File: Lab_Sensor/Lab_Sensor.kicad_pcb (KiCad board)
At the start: 2 copper layers, 94.2 x 66 mm, 31 parts, among them U1 ESP32-POE, U2 AM2302, U3 SSD1306, U4 INMP441

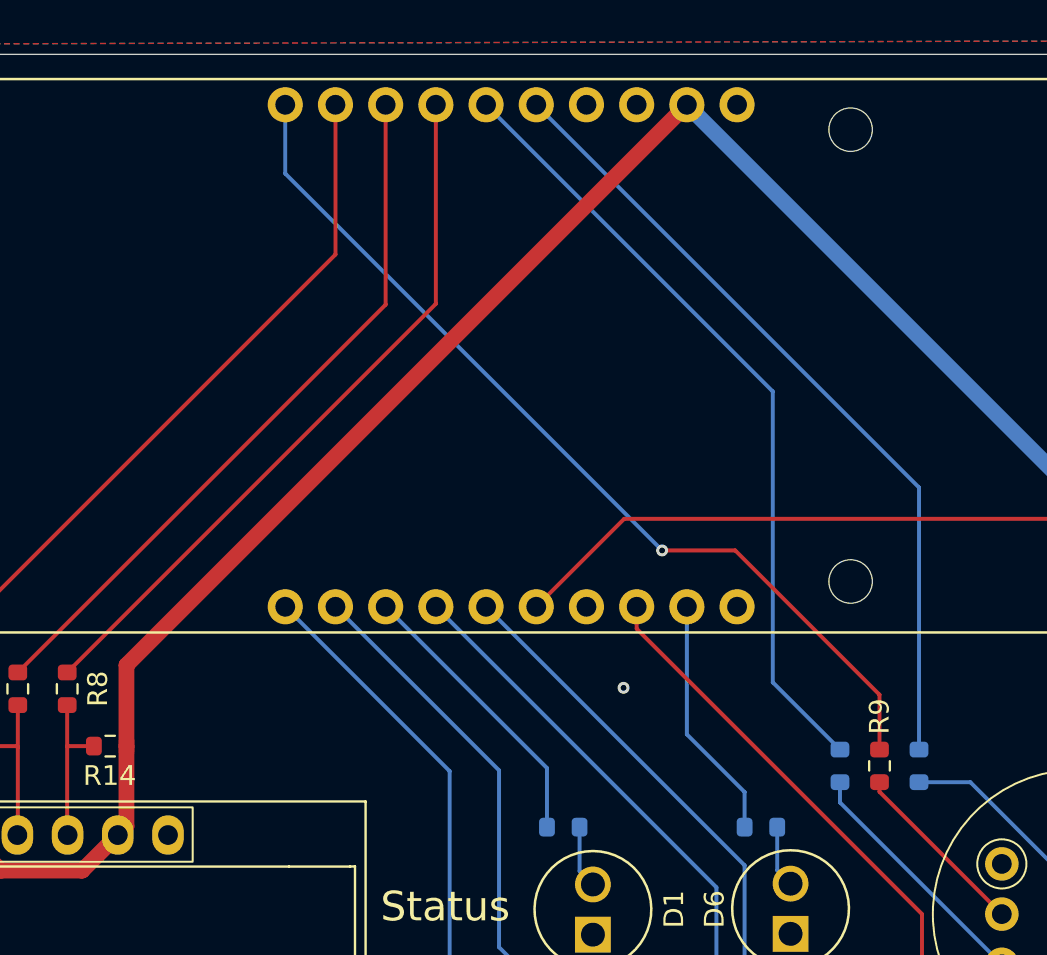
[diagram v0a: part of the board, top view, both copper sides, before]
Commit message: rerouted Input GPIO pins & added YAML file
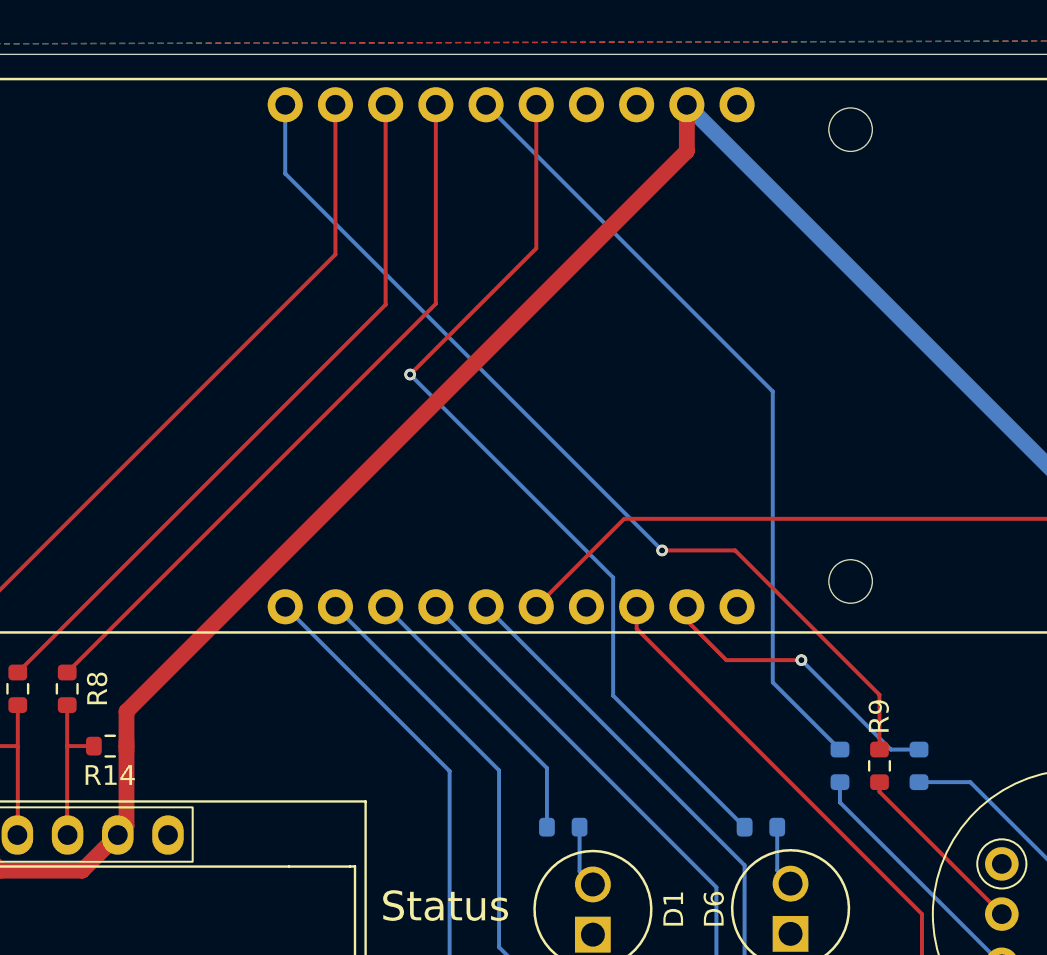
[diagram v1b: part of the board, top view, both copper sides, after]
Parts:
- turned R12 to 180 degrees
- turned R6 to -90 degrees
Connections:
- R12 pad 1: Net-(U1-GPI36) -> Net-(D6-PadA)
- R12 pad 2: Net-(D6-PadA) -> Net-(U1-GPIO0)
- R6 pad 1: Net-(U4-SD) -> Net-(U1-GPI36)
- R6 pad 2: Net-(U1-GPIO0) -> Net-(U4-SD)
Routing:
- net Net-(U1-GPIO0): track 40.6 -> 46.2 mm, vias 0 -> 1
- net Net-(U1-GPI36): track 12.4 -> 15.2 mm, vias 0 -> 1
- net GND: vias 1 -> 0

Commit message: switched pin 5 and 36
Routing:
- net GND: vias 0 -> 1
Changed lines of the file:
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@@
 		(net 1)
+	)
+	(via
+		(at 114.35 77.2)
+		(size 0.6)
+		(drill 0.3)
+		(layers "F.Cu" "B.Cu")
+		(free yes)
+		(net 2)
 	)
 	(segment
@@
 	)
 	(segment
-		(start 116.023 72.973)
-		(end 116.023 78.948)
+		(start 115.95 78.875)
+		(end 122.675 85.6)
 		(width 0.2)
 		(layer "B.Cu")
@@
 	)
 	(segment
-		(start 116.023 78.948)
-		(end 122.675 85.6)
+		(start 105.75 62.7)
+		(end 115.95 72.9)
 		(width 0.2)
 		(layer "B.Cu")
@@
 	)
 	(segment
-		(start 105.75 62.7)
-		(end 116.023 72.973)
-		(width 0.2)
-		(layer "B.Cu")
+		(start 115.95 72.9)
+		(end 115.95 78.875)
+		(width 0.2)
+		(layer "B.Cu")

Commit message: Grounded L/R
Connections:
- R11 pad 2: Net-(U1-GPIO1) -> Net-(U1-GPIO4)
- TP2 pad TP: Net-(U1-GPIO4) -> Net-(U1-GPIO1)
- U4 pad 1: unconnected-(U4-L/R-Pad1) -> GND
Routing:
- net Net-(U1-GPIO1): track 40.0 -> 50.2 mm, vias 0 -> 1
- net Net-(U1-GPIO4): track 42.0 -> 43.2 mm
- net GND: vias 1 -> 3
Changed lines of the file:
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@@
 	(net 22 "Net-(D2-PadA)")
 	(net 23 "Net-(D3-PadA)")
-	(net 24 "unconnected-(U4-L{slash}R-Pad1)")
-	(net 25 "Net-(U1-GPI36)")
-	(net 26 "Net-(U1-GPI35)")
-	(net 27 "Net-(U4-SCK)")
-	(net 28 "Net-(U4-SD)")
-	(net 29 "Net-(D5-PadA)")
-	(net 30 "Net-(D6-PadA)")
-	(net 31 "Net-(U4-WS)")
-	(net 32 "Net-(U1-GPIO0)")
-	(net 33 "Net-(U1-GPIO1)")
+	(net 24 "Net-(U1-GPI36)")
+	(net 25 "Net-(U1-GPI35)")
+	(net 26 "Net-(U4-SCK)")
+	(net 27 "Net-(U4-SD)")
+	(net 28 "Net-(D5-PadA)")
+	(net 29 "Net-(D6-PadA)")
+	(net 30 "Net-(U4-WS)")
+	(net 31 "Net-(U1-GPIO0)")
+	(net 32 "Net-(U1-GPIO1)")
 	(footprint "Custom_Parts:5002"
 		(layer "F.Cu")
@@
 			(layers "*.Cu" "*.Mask")
 			(remove_unused_layers no)
-			(net 6 "Net-(U1-GPIO4)")
+			(net 32 "Net-(U1-GPIO1)")
 			(pintype "passive")
 			(solder_mask_margin 0.102)
@@
 			(layers "*.Cu" "*.Mask")
 			(remove_unused_layers no)
-			(net 24 "unconnected-(U4-L{slash}R-Pad1)")
+			(net 2 "GND")
 			(pinfunction "L/R")
-			(pintype "no_connect")
+			(pintype "power_in")
 		)
 		(pad "2" thru_hole circle
@@
 			(layers "*.Cu" "*.Mask")
 			(remove_unused_layers no)
-			(net 31 "Net-(U4-WS)")
+			(net 30 "Net-(U4-WS)")
 			(pinfunction "WS")
 			(pintype "input")
@@
 			(layers "*.Cu" "*.Mask")
 			(remove_unused_layers no)
-			(net 27 "Net-(U4-SCK)")
+			(net 26 "Net-(U4-SCK)")
 			(pinfunction "SCK")
 			(pintype "input")
@@
 			(layers "*.Cu" "*.Mask")
 			(remove_unused_layers no)
-			(net 28 "Net-(U4-SD)")
+			(net 27 "Net-(U4-SD)")
 			(pinfunction "SD")
 			(pintype "input")
 		)
 		(embedded_fonts no)
+		(model "C:/Users/sidko/Desktop/GitHub/PCB-Projects/KiCad/Misc/INMP441.step"
+			(offset
+				(xyz 0 0 1.5)
+			)
+			(scale
+				(xyz 1 1 1)
+			)
+			(rotate
+				(xyz 90 -0 -180)
+			)
+		)
 	)
 	(footprint "MountingHole:MountingHole_2.2mm_M2"
@@
 			(layers "*.Cu" "*.Mask")
 			(remove_unused_layers no)
-			(net 26 "Net-(U1-GPI35)")
+			(net 25 "Net-(U1-GPI35)")
 			(pintype "passive")
 			(solder_mask_margin 0.102)
@@
 			(layers "*.Cu" "*.Mask")
 			(remove_unused_layers no)
-			(net 32 "Net-(U1-GPIO0)")
+			(net 31 "Net-(U1-GPIO0)")
 			(pinfunction "GPIO0")
 			(pintype "bidirectional")
@@
 			(layers "*.Cu" "*.Mask")
 			(remove_unused_layers no)
-			(net 33 "Net-(U1-GPIO1)")
+			(net 32 "Net-(U1-GPIO1)")
 			(pinfunction "GPIO1")
 			(pintype "bidirectional")
@@
 			(layers "*.Cu" "*.Mask")
 			(remove_unused_layers no)
-			(net 25 "Net-(U1-GPI36)")
+			(net 24 "Net-(U1-GPI36)")
 			(pinfunction "GPI36")
 			(pintype "input")
@@
 			(layers "*.Cu" "*.Mask")
 			(remove_unused_layers no)
-			(net 26 "Net-(U1-GPI35)")
+			(net 25 "Net-(U1-GPI35)")
 			(pinfunction "GPI35")
 			(pintype "input")
@@
 			(layers "*.Cu" "*.Mask")
 			(remove_unused_layers no)
-			(net 29 "Net-(D5-PadA)")
+			(net 28 "Net-(D5-PadA)")
 			(pinfunction "A")
 			(pintype "passive")
@@
 			(layers "F.Cu" "F.Mask" "F.Paste")
 			(roundrect_rratio 0.25)
-			(net 31 "Net-(U4-WS)")
+			(net 30 "Net-(U4-WS)")
 			(pintype "passive")
 		)
@@
 			(layers "*.Cu" "*.Mask")
 			(remove_unused_layers no)
-			(net 30 "Net-(D6-PadA)")
+			(net 29 "Net-(D6-PadA)")
 			(pinfunction "A")
 			(pintype "passive")
@@
 			(layers "B.Cu" "B.Mask" "B.Paste")
 			(roundrect_rratio 0.25)
-			(net 29 "Net-(D5-PadA)")
+			(net 28 "Net-(D5-PadA)")
 			(pintype "passive")
 		)
@@
 			(layers "B.Cu" "B.Mask" "B.Paste")
 			(roundrect_rratio 0.25)
-			(net 25 "Net-(U1-GPI36)")
+			(net 24 "Net-(U1-GPI36)")
 			(pintype "passive")
 		)
@@
 			(layers "B.Cu" "B.Mask" "B.Paste")
 			(roundrect_rratio 0.25)
-			(net 28 "Net-(U4-SD)")
+			(net 27 "Net-(U4-SD)")
 			(pintype "passive")
 		)
@@
 			(layers "B.Cu" "B.Mask" "B.Paste")
 			(roundrect_rratio 0.25)
-			(net 27 "Net-(U4-SCK)")
+			(net 26 "Net-(U4-SCK)")
 			(pintype "passive")
 		)
@@
 			(layers "B.Cu" "B.Mask" "B.Paste")
 			(roundrect_rratio 0.25)
-			(net 33 "Net-(U1-GPIO1)")
+			(net 6 "Net-(U1-GPIO4)")
 			(pintype "passive")
 		)
@@
 			(layers "B.Cu" "B.Mask" "B.Paste")
 			(roundrect_rratio 0.25)
-			(net 30 "Net-(D6-PadA)")
+			(net 29 "Net-(D6-PadA)")
 			(pintype "passive")
 		)
@@
 			(layers "B.Cu" "B.Mask" "B.Paste")
 			(roundrect_rratio 0.25)
-			(net 32 "Net-(U1-GPIO0)")
+			(net 31 "Net-(U1-GPIO0)")
 			(pintype "passive")
 		)
@@
 	)
 	(via
+		(at 108.25 52.2)
+		(size 0.6)
+		(drill 0.3)
+		(layers "F.Cu" "B.Cu")
+		(free yes)
+		(net 2)
+	)
+	(via
+		(at 110.85 52.3)
+		(size 0.6)
+		(drill 0.3)
+		(layers "F.Cu" "B.Cu")
+		(free yes)
+		(net 2)
+	)
+	(via
 		(at 114.35 77.2)
 		(size 0.6)
@@
 	(segment
 		(start 107.053 49.05)
-		(end 107.053 59.122)
+		(end 107.053 58.547)
 		(width 0.2)
 		(layer "F.Cu")
@@
 	)
 	(segment
-		(start 107.053 59.122)
+		(start 88.4 77.2)
 		(end 88.4 77.775)
 		(width 0.2)
@@
 	)
 	(segment
+		(start 107.053 58.547)
+		(end 88.4 77.2)
+		(width 0.2)
+		(layer "F.Cu")
+		(net 4)
+	)
+	(segment
 		(start 104.513 49.05)
 		(end 104.513 59.162)
@@
 	)
 	(segment
-		(start 101.973 49.05)
-		(end 101.973 56.627)
+		(start 124.05 71.127)
+		(end 124.05 78.225)
 		(width 0.2)
-		(layer "F.Cu")
+		(layer "B.Cu")
 		(net 6)
 	)
 	(segment
-		(start 101.973 56.627)
-		(end 77.65 80.95)
+		(start 124.05 78.225)
+		(end 127.5 81.675)
 		(width 0.2)
-		(layer "F.Cu")
+		(layer "B.Cu")
+		(net 6)
+	)
+	(segment
+		(start 101.973 49.05)
+		(end 124.05 71.127)
+		(width 0.2)
+		(layer "B.Cu")
 		(net 6)
 	)
@@
 		(width 0.2)
 		(layer "F.Cu")
-		(net 25)
+		(net 24)
 	)
 	(segment
@@
 		(width 0.2)
 		(layer "F.Cu")
-		(net 25)
+		(net 24)
 	)
 	(segment
@@
 		(width 0.2)
 		(layer "F.Cu")
-		(net 25)
+		(net 24)
 	)
 	(via
@@
 		(drill 0.3)
 		(layers "F.Cu" "B.Cu")
-		(net 25)
+		(net 24)
 	)
 	(segment
@@
 		(width 0.2)
 		(layer "B.Cu")
-		(net 25)
+		(net 24)
 	)
 	(segment
@@
 		(width 0.2)
 		(layer "B.Cu")
-		(net 25)
+		(net 24)
 	)
 	(segment
@@
 		(width 0.2)
 		(layer "F.Cu")
-		(net 26)
+		(net 25)
 	)
 	(segment
@@
 		(width 0.2)
 		(layer "F.Cu")
-		(net 26)
+		(net 25)
 	)
 	(segment
@@
 		(width 0.2)
 		(layer "F.Cu")
-		(net 26)
+		(net 25)
 	)
 	(segment
@@
 		(width 0.2)
 		(layer "B.Cu")
-		(net 27)
+		(net 26)
 	)
 	(segment
@@
 		(width 0.2)
 		(layer "B.Cu")
-		(net 27)
+		(net 26)
 	)
 	(segment
@@
 		(width 0.2)
 		(layer "B.Cu")
-		(net 28)
+		(net 27)
 	)
 	(segment
@@
 		(width 0.2)
 		(layer "B.Cu")
-		(net 28)
+		(net 27)
 	)
 	(segment
@@
 		(width 0.2)
 		(layer "B.Cu")
-		(net 29)
+		(net 28)
 	)
 	(segment
@@
 		(width 0.2)
 		(layer "B.Cu")
-		(net 29)
+		(net 28)
 	)
 	(segment
@@
 		(width 0.2)
 		(layer "B.Cu")
-		(net 30)
+		(net 29)
 	)
 	(segment
@@
 		(width 0.2)
 		(layer "B.Cu")
-		(net 30)
+		(net 29)
 	)
 	(segment
@@
 		(width 0.2)
 		(layer "F.Cu")
-		(net 31)
+		(net 30)
 	)
 	(segment
@@
 		(width 0.2)
 		(layer "F.Cu")
-		(net 31)
+		(net 30)
 	)
 	(segment
@@
 		(width 0.2)
 		(layer "F.Cu")
-		(net 32)
+		(net 31)
 	)
 	(segment
@@
 		(width 0.2)
 		(layer "F.Cu")
-		(net 32)
+		(net 31)
 	)
 	(via
@@
 		(drill 0.3)
 		(layers "F.Cu" "B.Cu")
-		(net 32)
+		(net 31)
 	)
 	(segment
@@
 		(width 0.2)
 		(layer "B.Cu")
-		(net 32)
+		(net 31)
 	)
 	(segment
@@
 		(width 0.2)
 		(layer "B.Cu")
-		(net 32)
+		(net 31)
 	)
 	(segment
@@
 		(width 0.2)
 		(layer "B.Cu")
+		(net 31)
+	)
+	(segment
+		(start 95.5 71.8)
+		(end 109.593 57.707)
+		(width 0.2)
+		(layer "F.Cu")
 		(net 32)
 	)
 	(segment
-		(start 109.593 49.05)
-		(end 124.1 63.557)
+		(start 109.593 57.707)
+		(end 109.593 49.05)
 		(width 0.2)
-		(layer "B.Cu")
-		(net 33)
+		(layer "F.Cu")
+		(net 32)
+	)
+	(via
+		(at 95.5 71.8)
+		(size 0.6)
+		(drill 0.3)
+		(layers "F.Cu" "B.Cu")
+		(net 32)
 	)
 	(segment
-		(start 124.1 78.275)
-		(end 127.5 81.675)
+		(start 77.65 80.95)
+		(end 86.8 71.8)
 		(width 0.2)
 		(layer "B.Cu")
-		(net 33)
+		(net 32)
 	)
 	(segment
-		(start 124.1 63.557)
-		(end 124.1 78.275)
+		(start 86.8 71.8)
+		(end 95.5 71.8)
 		(width 0.2)
 		(layer "B.Cu")
-		(net 33)
+		(net 32)
 	)
 	(zone
